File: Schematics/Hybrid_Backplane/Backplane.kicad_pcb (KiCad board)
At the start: 2 copper layers, 69.5 x 98.5 mm, 21 parts, among them J1 Edge Connector (SLOT 1), J2 Edge Connector (SLOT 2), J3 Edge Connector (SLOT 3), J4 Edge Connector (SLOT 4), J5 Edge Connector (SLOT 5), J6 Conn_01x06

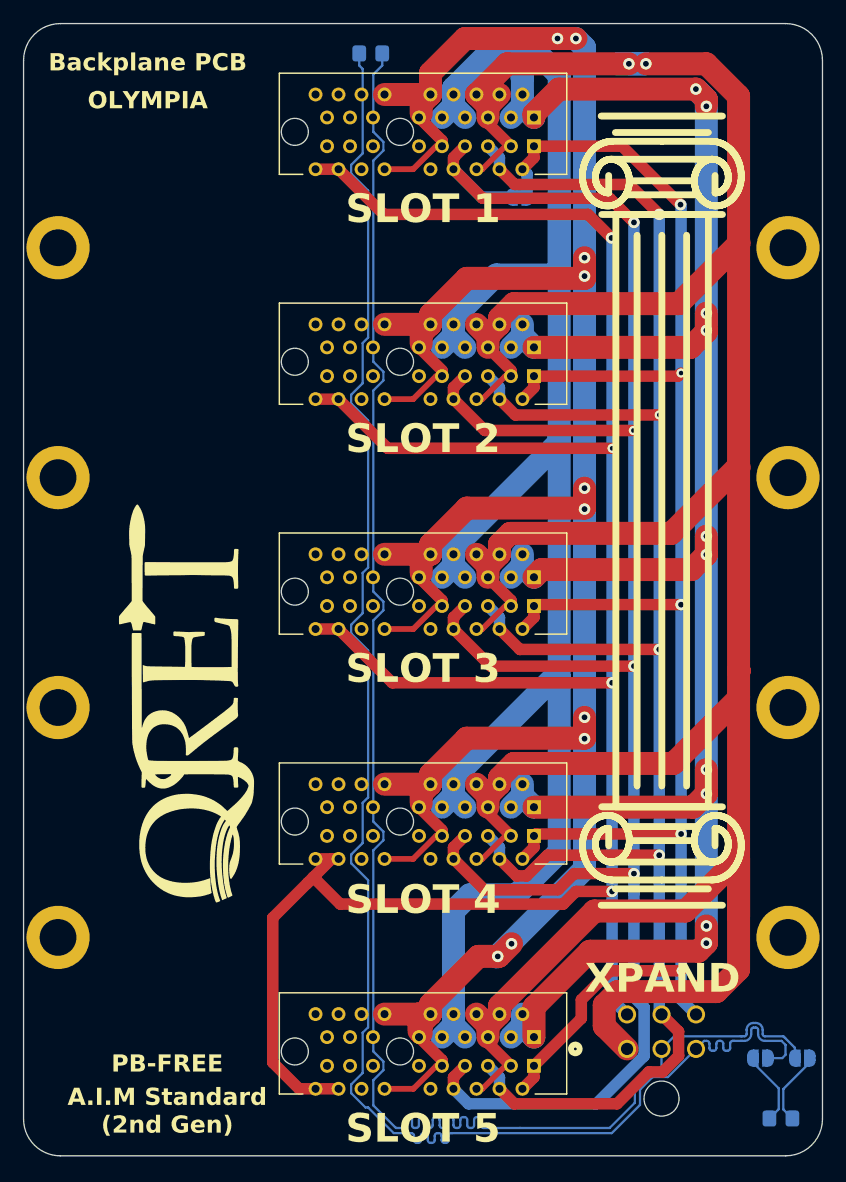
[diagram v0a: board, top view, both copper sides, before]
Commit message: add nano connector for xpand, adjust routing
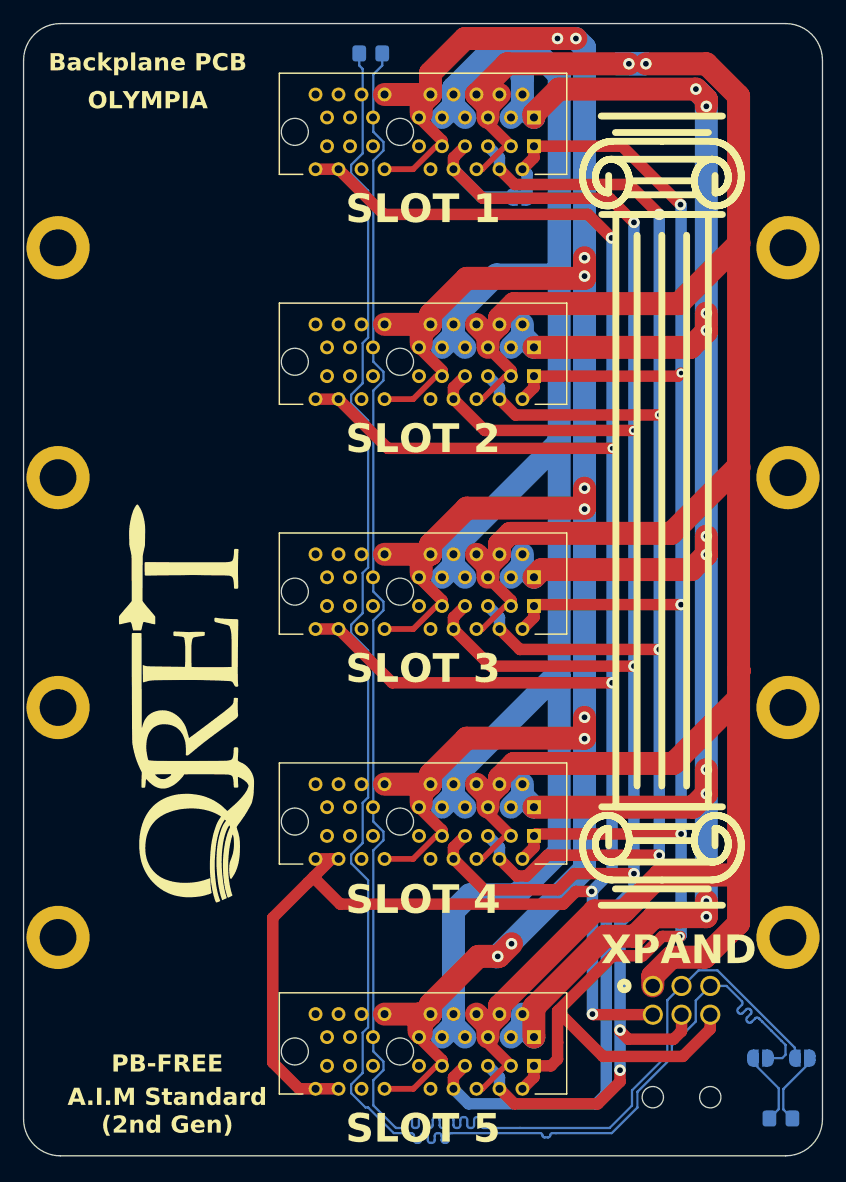
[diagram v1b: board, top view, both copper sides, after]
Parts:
- J6: footprint footprints:CONN_SD-43045-001_06_MOL -> footprints:CONN_SD-105314-100_06_MOL
- moved J6 5.92 mm to (54.7, 83.7)
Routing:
- net GNDA: track 281.3 -> 263.8 mm
- net 3.3V_A: track 156.5 -> 169.0 mm
- net CAN_N: track 149.7 -> 154.5 mm
- net CAN_P: track 149.7 -> 154.5 mm
- net 5.0V_A: track 164.0 -> 168.2 mm, vias 4 -> 6
- net 24V_A: track 207.6 -> 211.3 mm, vias 4 -> 5
- net BATT_A: track 186.1 -> 184.6 mm
- net 3.3V_B: track 178.8 -> 178.0 mm
